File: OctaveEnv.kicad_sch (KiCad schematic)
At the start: 0 parts

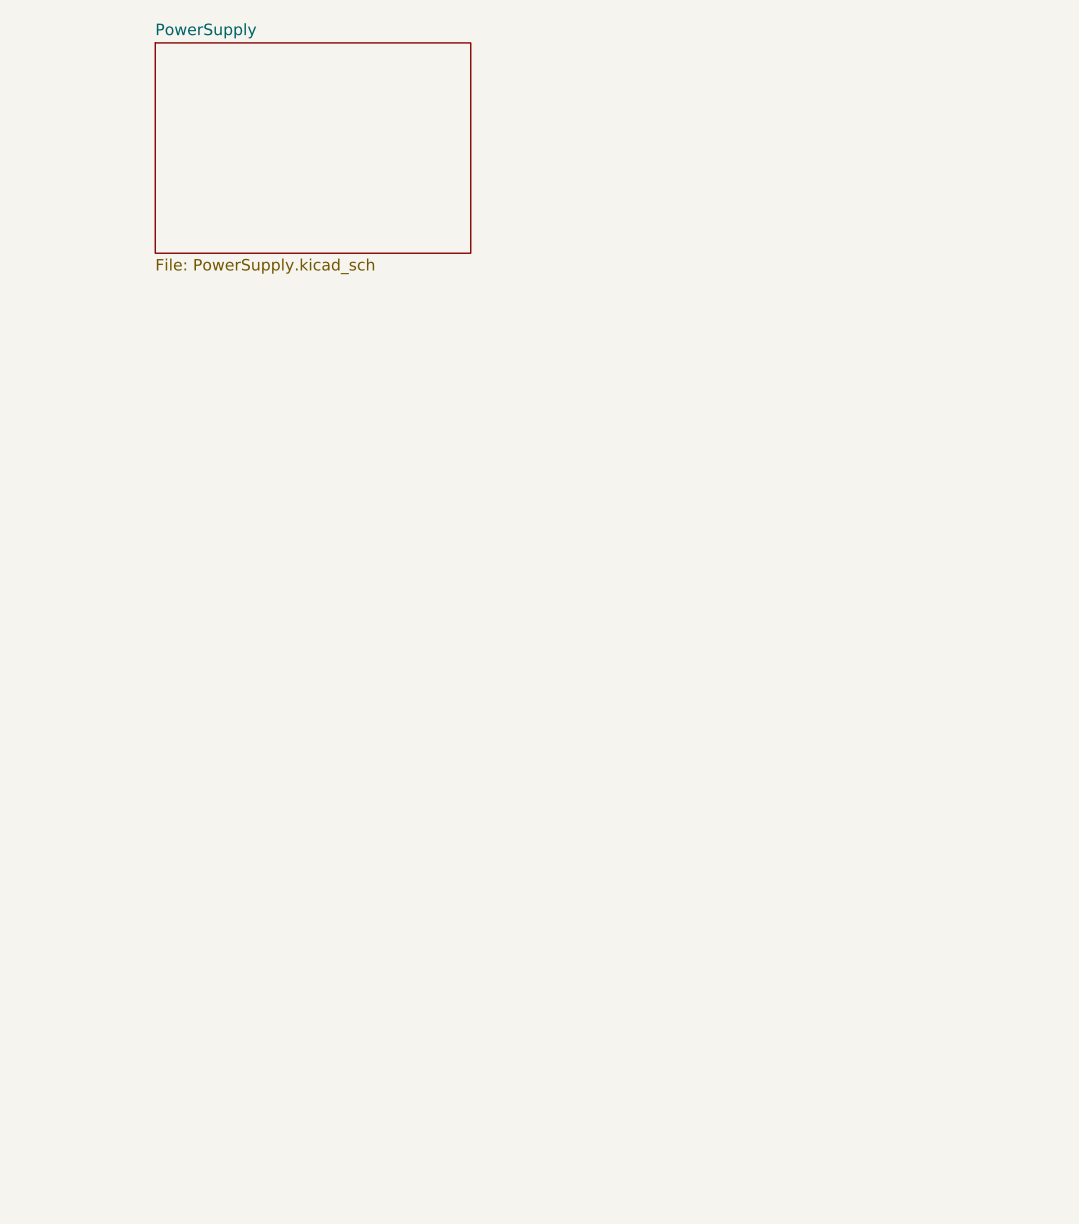
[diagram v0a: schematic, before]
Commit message: spice sim, start of schematic
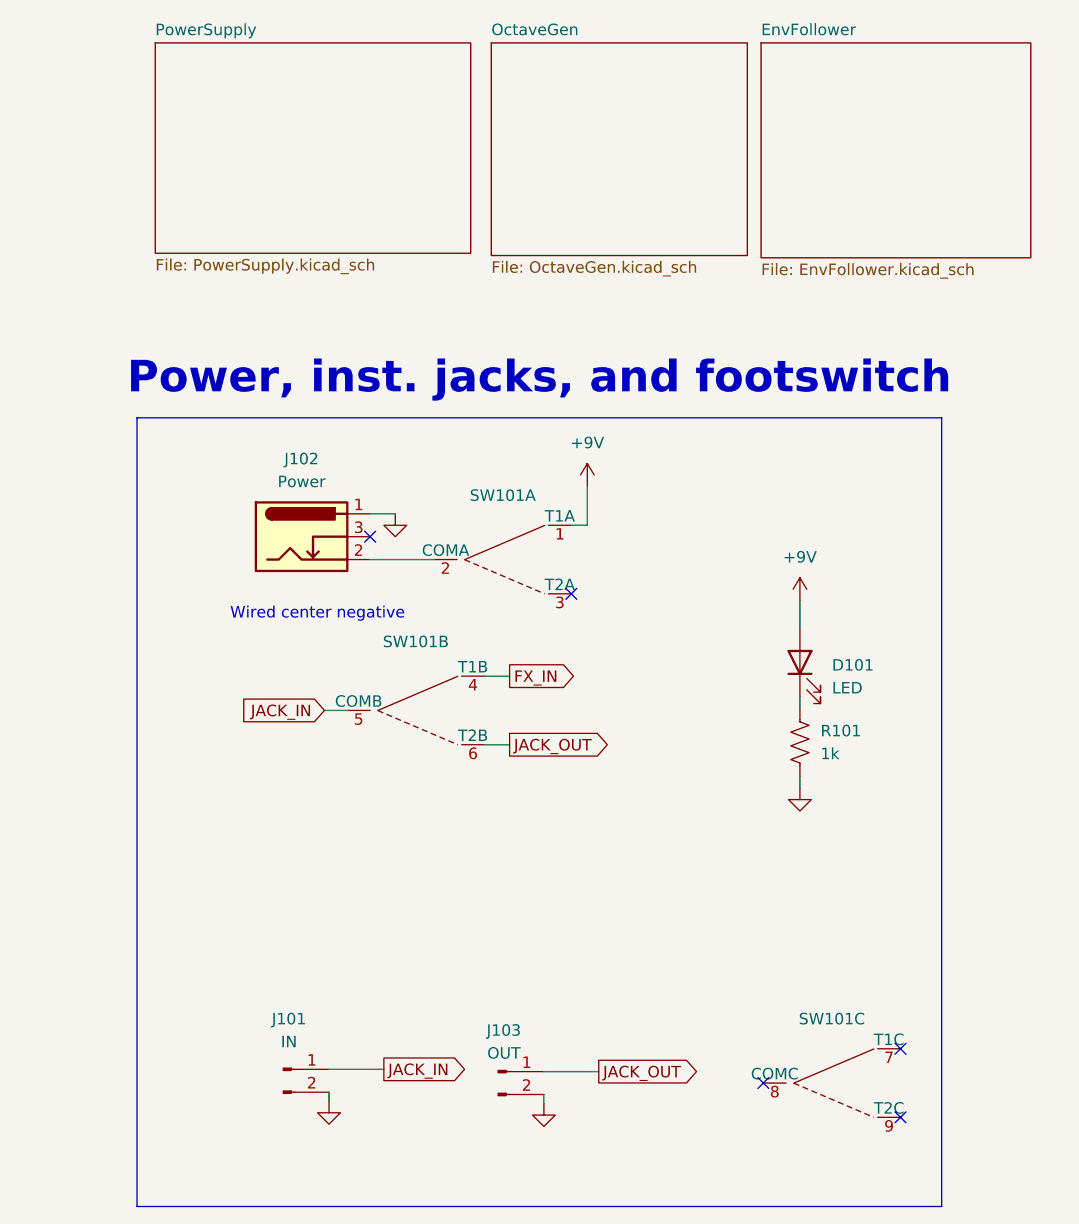
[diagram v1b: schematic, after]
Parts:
- added D101: LED, symbol Device:LED
- added J101: IN, Connector_PinHeader_2.54mm:PinHeader_1x02_P2.54mm_Vertical, symbol Connector:Conn_01x02_Pin
- added J102: Power, Connector_BarrelJack:BarrelJack_Kycon_KLDX-0202-xC_Horizontal, symbol Connector:Barrel_Jack_Switch
- added J103: OUT, Connector_PinHeader_2.54mm:PinHeader_1x02_P2.54mm_Vertical, symbol Connector:Conn_01x02_Pin
- added R101: 1k, symbol Device:R_US
- added SW101: ~, symbol Switch:SW_3PDT
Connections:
- new net: J102.2, SW101.2 (COMA)
- new net: D101.1 (K), R101.2
- new net +9V: D101.2 (A), SW101.1 (T1A)
- new net FX_IN: SW101.4 (T1B)
- new net GND: J101.2 (Pin_2), J102.1, J103.2 (Pin_2), R101.1
- new net JACK_IN: J101.1 (Pin_1), SW101.5 (COMB)
- new net JACK_OUT: J103.1 (Pin_1), SW101.6 (T2B)
- no-connect marks 0 -> 5
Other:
- added sheet EnvFollower (EnvFollower.kicad_sch)
- added sheet OctaveGen (OctaveGen.kicad_sch)
- note added: "Power, inst. jacks, and footswitch"
- note added: "Wired center negative"

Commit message: finished and consolidated schem
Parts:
- added C101: 100u, Capacitor_THT:CP_Radial_D5.0mm_P2.00mm, symbol Device:C_Polarized_US
- added C102, C103, C107, C108, C115, C116, C117, C118, C119, C120, C121: 100n, Capacitor_SMD:C_0805_2012Metric, symbol Device:C
- added C104: 470p, Capacitor_SMD:C_0805_2012Metric, symbol Device:C
- added C105, C106: 470u, Capacitor_THT:CP_Radial_D5.0mm_P2.00mm, symbol Device:C_Polarized_US
- added C109, C110, C111, C114, C124, C125, C126: 1u, Capacitor_SMD:C_0805_2012Metric, symbol Device:C
- added C112, C113, C123: 1n, Capacitor_SMD:C_0805_2012Metric, symbol Device:C
- added C122: 470n, Capacitor_SMD:C_0805_2012Metric, symbol Device:C
- added D102: PMEG3030, Diode_SMD:D_SOD-123, symbol Device:D_Schottky
- added D103, D104, D105: 1N4148, Diode_SMD:D_SOD-123, symbol Diode:1N4148
- added L101: 88uH, symbol Device:L
- added POT101, POT103, POT104: 100kB, Potentiometer_THT:Potentiometer_Alpha_RD901F-40-00D_Single_Vertical, symbol Device:R_Potentiometer_US
- added POT102, POT105: 100kA, Potentiometer_THT:Potentiometer_Alpha_RD901F-40-00D_Single_Vertical, symbol Device:R_Potentiometer_US
- added Q101: BC857, Package_TO_SOT_SMD:SOT-23, symbol Transistor_BJT:BC857
- added R102: 0.24R, Resistor_SMD:R_0805_2012Metric, symbol Device:R_US
- added R103: 51k, Resistor_SMD:R_0805_2012Metric, symbol Device:R_US
- added R104: 8k2, Resistor_SMD:R_0805_2012Metric, symbol Device:R_US
- added R105, R122: 10k, Resistor_SMD:R_0805_2012Metric, symbol Device:R_US
- added R106, R108, R111, R112, R118, R127: 47k, Resistor_SMD:R_0805_2012Metric, symbol Device:R_US
- added R107: 220k, Resistor_SMD:R_0805_2012Metric, symbol Device:R_US
- added R109, R114, R115, R128, R129, R130: 100k, Resistor_SMD:R_0805_2012Metric, symbol Device:R_US
- added R110, R125, R126: 1k, Resistor_SMD:R_0805_2012Metric, symbol Device:R_US
- added R113, R124, R131: 22k, Resistor_SMD:R_0805_2012Metric, symbol Device:R_US
- added R116, R117, R123: 680, Resistor_SMD:R_0805_2012Metric, symbol Device:R_US
- added R119: 33k, Resistor_SMD:R_0805_2012Metric, symbol Device:R_US
- added R120: 4k7, Resistor_SMD:R_0805_2012Metric, symbol Device:R_US
- added R121, R132: 470, Resistor_SMD:R_0805_2012Metric, symbol Device:R_US
- added U101: AZ34063U, Package_SO:SO-8_3.9x4.9mm_P1.27mm, symbol Regulator_Switching:AZ34063U
- added U102: L7805, PCM_4ms_Package_TO:TO-220-3_Vertical, symbol Regulator_Linear:L7805
- added U103, U106: TL074, Package_SO:SOIC-14_3.9x8.7mm_P1.27mm, symbol Amplifier_Operational:TL074
- added U104: 74HCT74, Package_SO:SO-14_3.9x8.65mm_P1.27mm, symbol 74xx:74HCT74
- added U105: LM13700, Package_SO:SOIC-16_3.9x9.9mm_P1.27mm, symbol Amplifier_Operational:LM13700
- added U107: TL072, Package_SO:SOIC-8_3.9x4.9mm_P1.27mm, symbol Amplifier_Operational:TL072
- D101: footprint (none) -> LED_THT:LED_D3.0mm
- R101: footprint (none) -> Resistor_SMD:R_0805_2012Metric
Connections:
- net +9V: now also C101.1, C102.1, C107.1, C116.1, C118.1, C120.1, R102.1, U101.6 (VCC), U102.1 (IN), U103.4 (V+), U105.11 (V+), U106.4 (V+), U107.8 (V+)
- net FX_IN: now also C111.1, R113.1
- net GND: now also C101.2, C102.2, C103.2, C105.1, C106.1, C107.2, C108.2, C112.2, C115.2, C116.2, C117.2, C118.2, C119.2, C120.2, C121.2, C125.2, L101.2, POT104.2, POT105.1, R103.1, R110.2, R112.2, R116.2, R117.2, R121.2, R124.2, R127.2, U102.2 (GND), U103.10 (+), U103.3 (+), U104.7 (GND), U106.12 (+), U106.3 (+), U107.3 (+), U107.5 (+)
- net JACK_OUT: now also POT105.2
- new net: U104.2 (D), U104.6 (~{Q})
- new net: C104.1, U101.3 (CAP)
- new net: U104.12 (D), U104.8 (~{Q})
- new net: D104.1 (K), R119.2, U106.5 (+)
- new net: D104.2 (A), U106.1
- new net: R122.1, U105.12, U107.2 (-)
- new net: R128.2, R129.2, R131.1, U107.6 (-)
- new net: C126.1, R131.2, U107.7
- new net: C114.1, U103.13 (-), U103.14
- new net: R114.2, R116.1, U105.13 (-)
- new net: C111.2, R105.1
- new net: R105.2, R107.1, U103.2 (-)
- new net: C112.1, POT102.2, U103.12 (+)
- new net: R127.1, R130.1, U106.9 (-)
- new net: POT103.1, R113.2, U106.2 (-)
- new net: POT103.2, R119.1
- new net: C125.1, R123.2, R124.1, U106.10 (+), U106.6 (-)
- new net: POT105.3, R132.2
- new net: R102.2, U101.1 (SWC), U101.7 (Sense), U101.8 (DRC)
- new net: Q101.2 (E), R118.2, R121.1
- new net: D102.1 (K), L101.1, U101.2 (SWE)
- new net: C110.2, POT101.3
- new net: C109.2, POT101.1
- new net: C122.2, R114.1
- new net: R109.2, R110.1, U103.5 (+)
- new net: C123.1, R115.2, R118.1, U106.13 (-)
- new net: POT102.1, R108.2, U103.8
- new net: POT101.2, R106.1
- new net: R103.2, R104.1, U101.5 (FB)
- new net: D103.1 (K), R111.1
- new net: C124.2, R126.1
- new net: POT104.3, R126.2, R129.1
- new net: D105.1 (K), R123.1
- new net: R106.2, R108.1, U103.9 (-)
- new net: C113.2, U103.6 (-)
- new net: C126.2, R132.1
- new net: D103.2 (A), U103.7
- new net: POT104.1, R125.2, R128.1
- new net: C123.2, Q101.1 (B), U106.14
- new net: D105.2 (A), U106.7
- new net: Q101.3 (C), R120.1
- new net: R120.2, U105.16
- new net: R117.1, U105.14 (+)
- new net +5V: C103.1, C115.1, R109.1, U102.3 (OUT), U104.1 (~{R}), U104.10 (~{S}), U104.13 (~{R}), U104.14 (VCC), U104.4 (~{S})
- new net -9V: C104.2, C105.2, C106.2, C108.1, C117.1, C119.1, C121.1, D102.2 (A), R104.2, U101.4 (GND), U103.11 (V-), U105.6 (V-), U106.11 (V-), U107.4 (V-)
- new net ENV: R115.1, R130.2, U106.8
- new net Edge: R111.2, R112.1, U104.3 (C)
- new net GTR_GAIN: C113.1, R107.2, R125.1, U103.1
- new net OCT_FULL: C114.2, C122.1
- new net OCT_VCA: C124.1, R122.2, U107.1
- new net SQR1: C109.1, U104.11 (C), U104.5 (Q)
- new net SQR2: C110.1, U104.9 (Q)
- no-connect marks 5 -> 17
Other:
- removed sheet EnvFollower
- removed sheet OctaveGen
- removed sheet PowerSupply
- note added: "DC jack, 1/4" jacks, and footswitch"
- note added: "Envelope follower"
- note added: "Envelope gain"
- note added: "Feedback voltage should be -1.25V per the datasheet"
- note added: "Frequency divider"
- note added: "Input gain stage"
- note added: "Mixer/ Tone Control"
- note added: "Oct1/Oct2 blend"
- note added: "Octave Generation"
- note added: "Output mixer"
- note added: "Output volume"
- note added: "Power supply"
- note added: "Tone control"
- note added: "VCA"
- note added: "Wet/dry blend"
- note removed: "Power, inst. jacks, and footswitch"
- moved on the sheet: D101, J101, J102, J103, R101, SW101A, SW101B, SW101C

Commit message: footprints assigned, ERC passing
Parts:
- L101: footprint (none) -> Inductor_SMD:L_Taiyo-Yuden_NR-80xx
- SW101: value ~ -> Stomp; footprint (none) -> Connector_Audio:StompSwitchBreakout_P200
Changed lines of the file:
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@@
 			)
 		)
-		(property "Footprint" ""
+		(property "Footprint" "Inductor_SMD:L_Taiyo-Yuden_NR-80xx"
 			(at 380.746 150.114 0)
 			(effects
@@
 			)
 		)
-		(property "Value" "~"
+		(property "Value" "Stomp"
 			(at 370.84 97.282 0)
 			(effects
@@
 			)
 		)
-		(property "Footprint" ""
+		(property "Footprint" "Connector_Audio:StompSwitchBreakout_P200"
 			(at 369.57 95.504 0)
 			(effects
@@
 			)
 		)
-		(property "Value" "~"
+		(property "Value" "Stomp"
 			(at 390.144 37.338 0)
 			(effects
@@
 			)
 		)
-		(property "Footprint" ""
+		(property "Footprint" "Connector_Audio:StompSwitchBreakout_P200"
 			(at 387.604 34.29 0)
 			(effects
@@
 			)
 		)
-		(property "Value" "~"
+		(property "Value" "Stomp"
 			(at 380.492 54.864 0)
 			(effects
@@
 			)
 		)
-		(property "Footprint" ""
+		(property "Footprint" "Connector_Audio:StompSwitchBreakout_P200"
 			(at 377.952 51.054 0)
 			(effects

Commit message: layout start
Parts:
- removed J102: Power, Connector_BarrelJack:BarrelJack_Kycon_KLDX-0202-xC_Horizontal, symbol Connector:Barrel_Jack_Switch
- added J102: PWR, Connector_PinHeader_2.54mm:PinHeader_1x02_P2.54mm_Vertical, symbol Connector:Conn_01x02_Pin
- L101: value 88uH -> 68uH; footprint Inductor_SMD:L_Taiyo-Yuden_NR-80xx -> Inductor_SMD:L_TDK_VLS6045EX_VLS6045AF
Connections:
- net GND: now also U103.12 (+), U103.5 (+), J102.2 (Pin_2); no longer U103.10 (+), U103.3 (+)
- net GTR_GAIN: now also U103.14; no longer U103.1
- net at R105.2, R107.1: now also U103.13 (-); no longer U103.2 (-)
- net at C112.1, POT102.2: now also U103.3 (+); no longer U103.12 (+)
- net at R109.2, R110.1: now also U103.10 (+); no longer U103.5 (+)
- net at POT102.1, R108.2: now also U103.7; no longer U103.8
- net at R106.2, R108.1: now also U103.6 (-); no longer U103.9 (-)
- net at SW101.2 (COMA): now also J102.1 (Pin_1)
- net at C113.2: now also U103.9 (-); no longer U103.6 (-)
- net at D103.2 (A): now also U103.8; no longer U103.7
- new net: C114.1, U103.1, U103.2 (-)
- no-connect marks 17 -> 16
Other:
- moved on the sheet: U103A, U103B, U103C, U103D

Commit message: routing and test points
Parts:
- added R133: LOOP, Resistor_THT:R_Axial_DIN0207_L6.3mm_D2.5mm_P5.08mm_Vertical, symbol Device:R_US
- added TP101: GTR GAIN, TestPoint:TestPoint_THTPad_D1.5mm_Drill0.7mm_VAL, symbol Connector:TestPoint
- added TP102: ENV, TestPoint:TestPoint_THTPad_D1.5mm_Drill0.7mm_VAL, symbol Connector:TestPoint
- added TP103: VCA IN, TestPoint:TestPoint_THTPad_D1.5mm_Drill0.7mm_VAL, symbol Connector:TestPoint
- added TP104: VCA_OUT, TestPoint:TestPoint_THTPad_D1.5mm_Drill0.7mm_VAL, symbol Connector:TestPoint
- added TP105: EDGE, TestPoint:TestPoint_THTPad_D1.5mm_Drill0.7mm_VAL, symbol Connector:TestPoint
- added TP106: SQR1, TestPoint:TestPoint_THTPad_D1.5mm_Drill0.7mm_VAL, symbol Connector:TestPoint
- added TP107: SQR2, TestPoint:TestPoint_THTPad_D1.5mm_Drill0.7mm_VAL, symbol Connector:TestPoint
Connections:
- net ENV: now also TP102.1
- net Edge: now also TP105.1
- net FX_IN: now also SW101.2 (T1B); no longer SW101.4 (T1B)
- net GND: now also R133.1, R133.2
- net GTR_GAIN: now also TP101.1
- net JACK_OUT: now also SW101.8 (T2B); no longer SW101.6 (T2B)
- net OCT_FULL: now also TP103.1
- net OCT_VCA: now also TP104.1
- net SQR1: now also TP106.1
- net SQR2: now also TP107.1
- net at J102.1 (Pin_1): now also SW101.4 (COMA); no longer SW101.2 (COMA)
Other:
- note added: "Test Points"
- moved on the sheet: C101, C102, C103, C104, C105, C106, C118, C119, C120, C121, C122, C123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

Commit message: smaller outline
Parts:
- R133: footprint Resistor_THT:R_Axial_DIN0207_L6.3mm_D2.5mm_P5.08mm_Vertical -> Resistor_THT:R_Axial_DIN0207_L6.3mm_D2.5mm_P7.62mm_Horizontal
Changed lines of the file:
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@@
 			)
 		)
-		(property "Footprint" "Resistor_THT:R_Axial_DIN0207_L6.3mm_D2.5mm_P5.08mm_Vertical"
+		(property "Footprint" "Resistor_THT:R_Axial_DIN0207_L6.3mm_D2.5mm_P7.62mm_Horizontal"
 			(at 40.386 239.776 90)
 			(effects
